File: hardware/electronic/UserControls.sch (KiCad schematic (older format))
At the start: 25 parts, among them J3 PTT Button, J4 Top Controls, Q1 TSM850N06CX, SW1 BTN_LEFT, SW2 BTN_UP, SW3 BTN_SELECT, SW4 BTN_DOWN, SW5 BTN_RIGHT, U8 MCP23008_SO

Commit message: Rescued schematic symbols since LMRHAT.lib didn't get saved
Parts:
- LCD1: symbol adafruit:JD-T1800 -> LMRHAT-rescue:JD-T1800-adafruit
- Q1: symbol LMRHAT:TSM850N06CX -> LMRHAT-rescue:TSM850N06CX-LMRHAT
- SW1, SW2, SW3, SW4, SW5: footprint LMRHAT:SW_PUSH_6mm_SEP -> Button_Switch_SMD:SW_SPST_PTS645
- U8: symbol adafruit:MCP23008_SO -> LMRHAT-rescue:MCP23008_SO-adafruit
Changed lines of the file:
@@
 $EndDescr
 $Comp
-L LMRHAT:GND #PWR0110
+L LMRHAT-rescue:GND-LMRHAT #PWR0110
 U 1 1 5C02E7BF
 P 1550 4950
@@
 F 0 "SW1" H 3100 3285 50  0000 C CNN
 F 1 "BTN_LEFT" H 3100 3194 50  0000 C CNN
-F 2 "LMRHAT:SW_PUSH_6mm_SEP" H 3100 3200 50  0001 C CNN
+F 2 "Button_Switch_SMD:SW_SPST_PTS645" H 3100 3200 50  0001 C CNN
 F 3 "" H 3100 3200 50  0001 C CNN
 	1    3100 3000
@@
 F 0 "SW3" H 3100 2685 50  0000 C CNN
 F 1 "BTN_SELECT" H 3100 2594 50  0000 C CNN
-F 2 "LMRHAT:SW_PUSH_6mm_SEP" H 3100 2600 50  0001 C CNN
+F 2 "Button_Switch_SMD:SW_SPST_PTS645" H 3100 2600 50  0001 C CNN
 F 3 "" H 3100 2600 50  0001 C CNN
 	1    3100 2400
@@
 F 0 "SW5" H 3100 3885 50  0000 C CNN
 F 1 "BTN_RIGHT" H 3100 3794 50  0000 C CNN
-F 2 "LMRHAT:SW_PUSH_6mm_SEP" H 3100 3800 50  0001 C CNN
+F 2 "Button_Switch_SMD:SW_SPST_PTS645" H 3100 3800 50  0001 C CNN
 F 3 "" H 3100 3800 50  0001 C CNN
 	1    3100 3600
@@
 F 0 "SW4" H 3100 2085 50  0000 C CNN
 F 1 "BTN_DOWN" H 3100 1994 50  0000 C CNN
-F 2 "LMRHAT:SW_PUSH_6mm_SEP" H 3100 2000 50  0001 C CNN
-F 3 "" H 3100 2000 50  0001 C CNN
+F 2 "Button_Switch_SMD:SW_SPST_PTS645" H 3100 2000 50  0001 C CNN
+F 3 "https://www.ckswitches.com/media/1471/pts645.pdf" H 3100 2000 50  0001 C CNN
 	1    3100 1800
 	1    0    0    -1
@@
 BTN_DOWN
 $Comp
-L LMRHAT:GND #PWR0115
+L LMRHAT-rescue:GND-LMRHAT #PWR0115
 U 1 1 5C02E881
 P 1300 1900
@@
 $EndComp
 $Comp
-L adafruit:MCP23008_SO U8
+L LMRHAT-rescue:MCP23008_SO-adafruit U8
 U 1 1 5C02E8A1
 P 3400 5500
@@
 	3400 4650 3400 4700
 $Comp
-L LMRHAT:GND #PWR0116
+L LMRHAT-rescue:GND-LMRHAT #PWR0116
 U 1 1 5C02E8BE
 P 3400 6450
@@
 $EndComp
 $Comp
-L adafruit:JD-T1800 LCD?
+L LMRHAT-rescue:JD-T1800-adafruit LCD?
 U 1 1 5C198738
 P 9200 2850
@@
 $EndComp
 $Comp
-L LMRHAT:GND #PWR?
+L LMRHAT-rescue:GND-LMRHAT #PWR?
 U 1 1 5C19873E
 P 8300 3450
@@
 Connection ~ 8300 3150
 $Comp
-L LMRHAT:GND #PWR?
+L LMRHAT-rescue:GND-LMRHAT #PWR?
 U 1 1 5C198757
 P 7000 2850
@@
 LCD_DC
 $Comp
-L LMRHAT:TSM850N06CX Q?
+L LMRHAT-rescue:TSM850N06CX-LMRHAT Q?
 U 1 1 5C198764
 P 8300 1550
@@
 BKLIGHT
 $Comp
-L LMRHAT:GND #PWR?
+L LMRHAT-rescue:GND-LMRHAT #PWR?
 U 1 1 5C198773
 P 8900 1850
@@
 Connection ~ 2800 4700
 $Comp
-L LMRHAT:GND #PWR0120
+L LMRHAT-rescue:GND-LMRHAT #PWR0120
 U 1 1 5C1BC79F
 P 2400 5000
@@
 $EndComp
 $Comp
-L LMRHAT:GND #PWR0121
+L LMRHAT-rescue:GND-LMRHAT #PWR0121
 U 1 1 5C1C5A0D
 P 2400 6500
@@
 F 0 "SW2" H 3100 1485 50  0000 C CNN
 F 1 "BTN_UP" H 3100 1394 50  0000 C CNN
-F 2 "LMRHAT:SW_PUSH_6mm_SEP" H 3100 1400 50  0001 C CNN
-F 3 "" H 3100 1400 50  0001 C CNN
+F 2 "Button_Switch_SMD:SW_SPST_PTS645" H 3100 1400 50  0001 C CNN
+F 3 "https://www.ckswitches.com/media/1471/pts645.pdf" H 3100 1400 50  0001 C CNN
 	1    3100 1200
 	1    0    0    -1

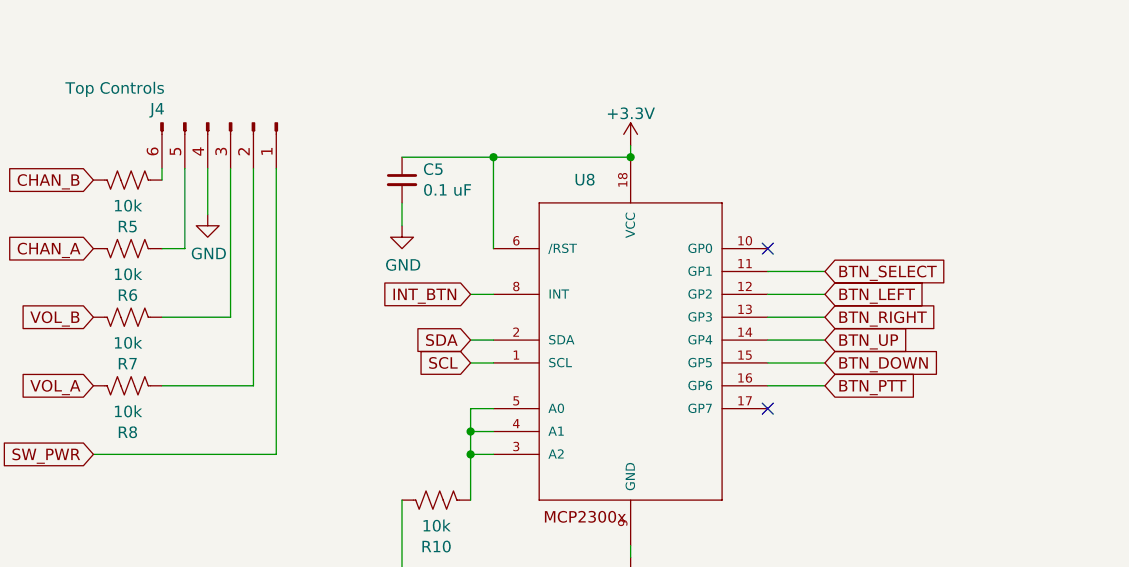
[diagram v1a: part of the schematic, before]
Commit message: Updated layout and schematic to match board dimensions of 50x80mm
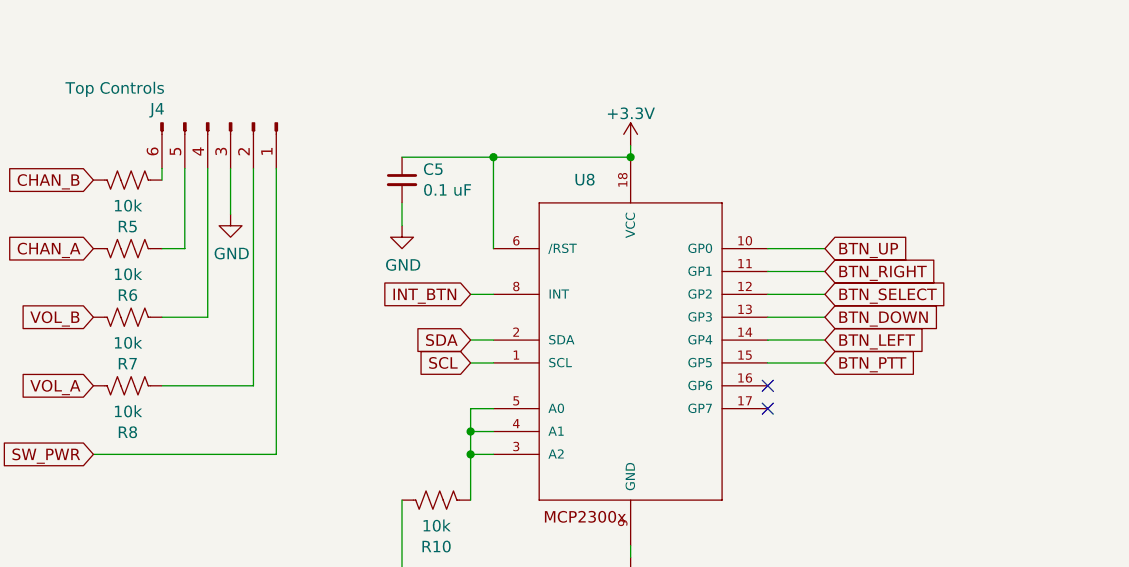
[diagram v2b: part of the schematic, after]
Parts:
- J4: footprint Connector_JST:JST_EH_B06B-EH-A_1x06_P2.50mm_Vertical -> Connector_PinHeader_2.54mm:PinHeader_2x03_P2.54mm_Vertical
- SW1, SW2, SW3, SW4, SW5: footprint Button_Switch_SMD:SW_SPST_PTS645 -> Button_Switch_THT:SW_PUSH_6mm_H5mm
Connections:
- net BTN_DOWN: now also U8.13 (GP3); no longer U8.15 (GP5)
- net BTN_LEFT: now also U8.14 (GP4); no longer U8.12 (GP2)
- net BTN_PTT: now also U8.15 (GP5); no longer U8.16 (GP6)
- net BTN_RIGHT: now also U8.11 (GP1); no longer U8.13 (GP3)
- net BTN_SELECT: now also U8.12 (GP2); no longer U8.11 (GP1)
- net BTN_UP: now also U8.10 (GP0); no longer U8.14 (GP4)
- net GND: now also J4.3 (Pin_3); no longer J4.4 (Pin_4)
- net at R7.1: now also J4.4 (Pin_4); no longer J4.3 (Pin_3)
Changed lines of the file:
@@
 L LMRHAT-rescue:GND-LMRHAT #PWR0110
 U 1 1 5C02E7BF
-P 1550 4950
-F 0 "#PWR0110" H 1550 4700 50  0001 C CNN
-F 1 "GND" H 1555 4777 50  0000 C CNN
-F 2 "" H 1550 4950 50  0000 C CNN
-F 3 "" H 1550 4950 50  0000 C CNN
-	1    1550 4950
-	1    0    0    -1
-$EndComp
-Wire Wire Line
-	1550 4950 1550 4750
+P 1650 4950
+F 0 "#PWR0110" H 1650 4700 50  0001 C CNN
+F 1 "GND" H 1655 4777 50  0000 C CNN
+F 2 "" H 1650 4950 50  0000 C CNN
+F 3 "" H 1650 4950 50  0000 C CNN
+	1    1650 4950
+	1    0    0    -1
+$EndComp
+Wire Wire Line
+	1650 4950 1650 4750
 $Comp
 L Device:R_US R5
@@
 F 0 "SW1" H 3100 3285 50  0000 C CNN
 F 1 "BTN_LEFT" H 3100 3194 50  0000 C CNN
-F 2 "Button_Switch_SMD:SW_SPST_PTS645" H 3100 3200 50  0001 C CNN
+F 2 "Button_Switch_THT:SW_PUSH_6mm_H5mm" H 3100 3200 50  0001 C CNN
 F 3 "" H 3100 3200 50  0001 C CNN
 	1    3100 3000
@@
 F 0 "SW3" H 3100 2685 50  0000 C CNN
 F 1 "BTN_SELECT" H 3100 2594 50  0000 C CNN
-F 2 "Button_Switch_SMD:SW_SPST_PTS645" H 3100 2600 50  0001 C CNN
+F 2 "Button_Switch_THT:SW_PUSH_6mm_H5mm" H 3100 2600 50  0001 C CNN
 F 3 "" H 3100 2600 50  0001 C CNN
 	1    3100 2400
@@
 F 0 "SW5" H 3100 3885 50  0000 C CNN
 F 1 "BTN_RIGHT" H 3100 3794 50  0000 C CNN
-F 2 "Button_Switch_SMD:SW_SPST_PTS645" H 3100 3800 50  0001 C CNN
+F 2 "Button_Switch_THT:SW_PUSH_6mm_H5mm" H 3100 3800 50  0001 C CNN
 F 3 "" H 3100 3800 50  0001 C CNN
 	1    3100 3600
@@
 F 0 "SW4" H 3100 2085 50  0000 C CNN
 F 1 "BTN_DOWN" H 3100 1994 50  0000 C CNN
-F 2 "Button_Switch_SMD:SW_SPST_PTS645" H 3100 2000 50  0001 C CNN
+F 2 "Button_Switch_THT:SW_PUSH_6mm_H5mm" H 3100 2000 50  0001 C CNN
 F 3 "https://www.ckswitches.com/media/1471/pts645.pdf" H 3100 2000 50  0001 C CNN
 	1    3100 1800
@@
 User Controls
 $Comp
-L Connector:Conn_01x06_Male J4
-U 1 1 5C02E89A
-P 1650 4550
-F 0 "J4" V 1590 4262 50  0000 R CNN
-F 1 "Top Controls" V 1499 4262 50  0000 R CNN
-F 2 "Connector_JST:JST_EH_B06B-EH-A_1x06_P2.50mm_Vertical" H 1650 4550 50  0001 C CNN
-F 3 "http://www.jst-mfg.com/product/pdf/eng/eEH.pdf" H 1650 4550 50  0001 C CNN
-	1    1650 4550
-	0    1    1    0
-$EndComp
-$Comp
 L LMRHAT-rescue:MCP23008_SO-adafruit U8
 U 1 1 5C02E8A1
@@
 	1    0    0    -1
 $EndComp
-Text GLabel 4250 5700 2    50   Input ~ 0
+Text GLabel 4250 5600 2    50   Input ~ 0
 BTN_PTT
+Text GLabel 4250 5300 2    50   Input ~ 0
+BTN_SELECT
+Text GLabel 4250 5500 2    50   Input ~ 0
+BTN_LEFT
 Text GLabel 4250 5200 2    50   Input ~ 0
-BTN_SELECT
-Text GLabel 4250 5300 2    50   Input ~ 0
-BTN_LEFT
+BTN_RIGHT
+Text GLabel 4250 5100 2    50   Input ~ 0
+BTN_UP
 Text GLabel 4250 5400 2    50   Input ~ 0
-BTN_RIGHT
-Text GLabel 4250 5500 2    50   Input ~ 0
-BTN_UP
-Text GLabel 4250 5600 2    50   Input ~ 0
 BTN_DOWN
 Wire Wire Line
@@
 Wire Wire Line
 	4000 5400 4250 5400
-Wire Wire Line
-	4000 5500 4250 5500
-Wire Wire Line
-	4000 5600 4250 5600
 $Comp
 L power:+3.3V #Vpi0103
@@
 Text GLabel 2700 5600 0    50   Input ~ 0
 SCL
-NoConn ~ 4000 5100
+NoConn ~ 4000 5700
 NoConn ~ 1850 750
 $Comp
@@
 Wire Wire Line
 	2800 4700 3400 4700
-Connection ~ 3400 4700
 Wire Wire Line
 	2400 4700 2800 4700
@@
 $EndComp
 Wire Wire Line
-	1650 5400 1650 4750
-Wire Wire Line
-	1350 5400 1650 5400
-Wire Wire Line
 	1750 5700 1750 4750
 Wire Wire Line
@@
 F 0 "SW2" H 3100 1485 50  0000 C CNN
 F 1 "BTN_UP" H 3100 1394 50  0000 C CNN
-F 2 "Button_Switch_SMD:SW_SPST_PTS645" H 3100 1400 50  0001 C CNN
-F 3 "https://www.ckswitches.com/media/1471/pts645.pdf" H 3100 1400 50  0001 C CNN
+F 2 "Button_Switch_THT:SW_PUSH_6mm_H5mm" H 3100 1400 50  0001 C CNN
+F 3 "" H 3100 1400 50  0001 C CNN
 	1    3100 1200
 	1    0    0    -1
@@
 Wire Wire Line
 	1300 1900 1300 1850
-Wire Wire Line
-	4000 5700 4250 5700
+Connection ~ 3400 4700
+Wire Wire Line
+	4000 5100 4250 5100
+Wire Wire Line
+	4000 5500 4250 5500
+Wire Wire Line
+	4250 5600 4000 5600
+$Comp
+L Connector:Conn_01x06_Male J4
+U 1 1 5C02E89A
+P 1650 4550
+F 0 "J4" V 1590 4262 50  0000 R CNN
+F 1 "Top Controls" V 1499 4262 50  0000 R CNN
+F 2 "Connector_PinHeader_2.54mm:PinHeader_2x03_P2.54mm_Vertical" H 1650 4550 50  0001 C CNN
+F 3 "" H 1650 4550 50  0001 C CNN
+	1    1650 4550
+	0    1    1    0
+$EndComp
+Wire Wire Line
+	1350 5400 1550 5400
+Wire Wire Line
+	1550 5400 1550 4750
 $EndSCHEMATC
